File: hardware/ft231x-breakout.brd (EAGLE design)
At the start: 26.7 x 15.2 mm, 27 parts, among them Q1 2N7002PW, U1 FT231XS

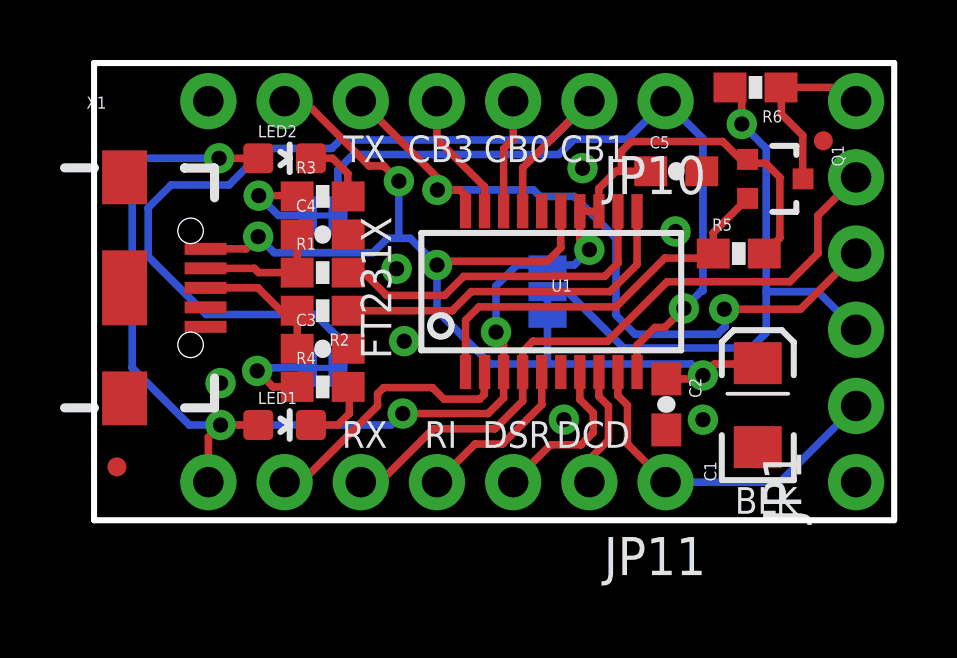
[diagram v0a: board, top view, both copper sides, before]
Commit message: Updated USB with Staking vias
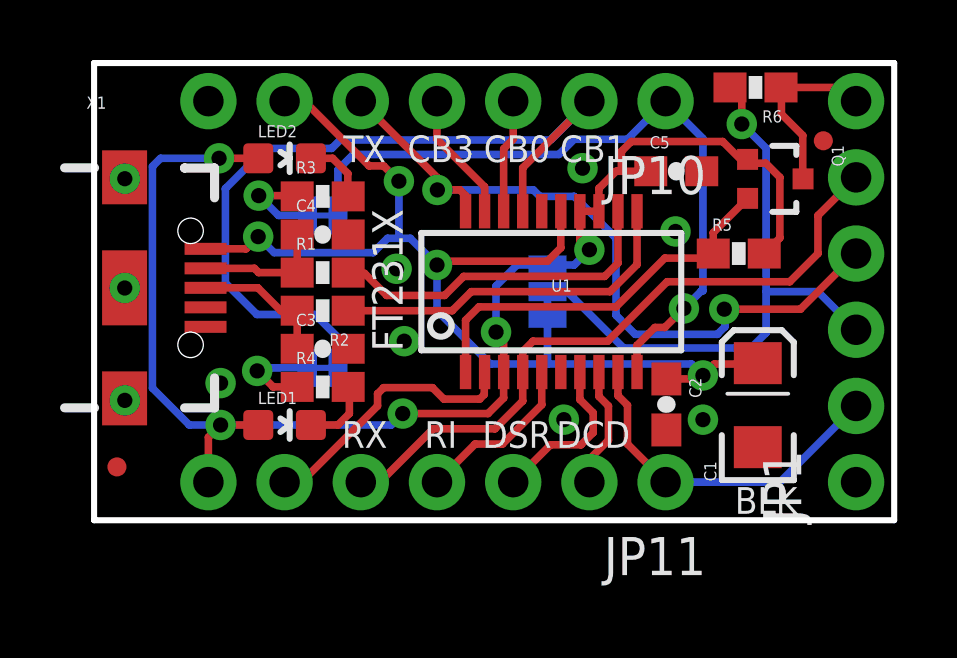
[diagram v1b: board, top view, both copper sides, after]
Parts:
- removed JP2: LOGO-SFENW2, SparkFun-Aesthetics:SFE-NEW-WEB
- added LOGO1: SFE_LOGO_NAME.1_INCH, SparkFun-Aesthetics:SFE_LOGO_NAME_.1
- moved FRAME1 11.7 mm to (-7.62, -12.7)
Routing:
- net RXLED: track 32.6 -> 28.4 mm
- net 3.3V: track 49.5 -> 48.6 mm
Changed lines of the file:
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@@
 <setting verticaltext="up"/>
 </settings>
-<grid distance="0.05" unitdist="inch" unit="inch" style="lines" multiple="1" display="yes" altdistance="0.005" altunitdist="inch" altunit="inch"/>
+<grid distance="0.05" unitdist="inch" unit="inch" style="lines" multiple="1" display="yes" altdistance="0.0001" altunitdist="inch" altunit="inch"/>
 <layers>
 <layer number="1" name="Top" color="4" fill="1" visible="yes" active="yes"/>
@@
 <text x="11.557" y="3.302" size="0.889" layer="21" font="vector" ratio="15" rot="R180" align="bottom-center">RI</text>
 <text x="9.017" y="3.302" size="0.889" layer="21" font="vector" ratio="15" rot="R180" align="bottom-center">RX</text>
-<text x="8.89" y="7.747" size="1.016" layer="21" font="vector" ratio="15" rot="R90" align="top-center">FT231X</text>
+<text x="9.271" y="8.001" size="1.016" layer="21" font="vector" ratio="15" rot="R90" align="top-center">FT231X</text>
 <text x="15.113" y="5.969" size="1.016" layer="22" font="vector" ratio="15" rot="MR0" align="top-center">5V</text>
 <text x="14.986" y="9.271" size="1.016" layer="22" font="vector" ratio="15" rot="MR180" align="top-center">3.3</text>
@@
 </autorouter>
 <elements>
-<element name="FRAME1" library="SparkFun-Aesthetics" package="CREATIVE_COMMONS" value="FRAME-LETTER" x="0" y="-3.81"/>
+<element name="FRAME1" library="SparkFun-Aesthetics" package="CREATIVE_COMMONS" value="FRAME-LETTER" x="-7.62" y="-12.7"/>
 <element name="U1" library="SparkFun-DigitalIC" package="SSOP20_L" value="FT231XS" x="15.24" y="7.62" smashed="yes">
 <attribute name="NAME" x="15.24" y="7.62" size="0.4064" layer="25"/>
-<attribute name="VALUE" x="15.24" y="6.35" size="0.4064" layer="27"/>
+<attribute name="VALUE" value="FTS31XS-U" x="15.24" y="6.35" size="0.4064" layer="27"/>
+<attribute name="PROD_ID" value="IC-11524" x="15.24" y="7.62" size="1.778" layer="27" display="off"/>
 </element>
 <element name="C2" library="SparkFun-Capacitors" package="0603-CAP" value="0.1uF" x="19.0754" y="3.8608" rot="R270">
@@
 <attribute name="VALUE" value="10K" x="22.0472" y="14.4272" size="1.778" layer="27" rot="R180" display="off"/>
 </element>
-<element name="JP2" library="SparkFun-Aesthetics" package="SFE-NEW-WEB" value="LOGO-SFENW2" x="13.843" y="5.842" rot="MR0"/>
 <element name="U$1" library="SparkFun-Aesthetics" package="OSHW-LOGO-S" value="OSHW-LOGOS" x="19.304" y="7.493" smashed="yes" rot="MR0"/>
 <element name="JP3" library="SparkFun-Aesthetics" package="MICRO-FIDUCIAL" value="FIDUCIALUFIDUCIAL" x="0.762" y="1.778"/>
 <element name="JP4" library="SparkFun-Aesthetics" package="MICRO-FIDUCIAL" value="FIDUCIALUFIDUCIAL" x="24.3078" y="12.6492"/>
+<element name="LOGO1" library="SparkFun-Aesthetics" package="SFE_LOGO_NAME_.1" value="SFE_LOGO_NAME.1_INCH" x="12.7" y="5.588" rot="MR0"/>
 </elements>
 <signals>
@@
 <via x="20.2946" y="3.3528" extent="1-16" drill="0.508"/>
 <via x="10.0838" y="8.382" extent="1-16" drill="0.508"/>
+<via x="1.02108125" y="7.741921875" extent="1-16" drill="0.508"/>
+<via x="1.023621875" y="3.995421875" extent="1-16" drill="0.508"/>
+<via x="1.023621875" y="11.384284375" extent="1-16" drill="0.508"/>
 </signal>
 <signal name="VCC">
@@
 <wire x1="22.86" y1="9.4116" x2="22.3384" y2="8.89" width="0.254" layer="1"/>
 <wire x1="4.2164" y1="3.175" x2="3.175" y2="3.175" width="0.254" layer="16"/>
-<wire x1="3.175" y1="3.175" x2="1.27" y2="5.08" width="0.254" layer="16"/>
-<wire x1="1.27" y1="5.08" x2="1.27" y2="11.6586" width="0.254" layer="16"/>
-<wire x1="1.27" y1="11.6586" x2="1.6764" y2="12.065" width="0.254" layer="16"/>
-<wire x1="1.6764" y1="12.065" x2="4.1656" y2="12.065" width="0.254" layer="16"/>
 <wire x1="9.906" y1="3.175" x2="10.287" y2="3.556" width="0.254" layer="16"/>
 <wire x1="3.81" y1="1.27" x2="3.81" y2="2.7686" width="0.254" layer="1"/>
 <wire x1="3.81" y1="2.7686" x2="4.2164" y2="3.175" width="0.254" layer="1"/>
+<wire x1="3.175" y1="3.175" x2="1.945640625" y2="4.404359375" width="0.254" layer="16"/>
+<wire x1="1.945640625" y1="4.404359375" x2="1.945640625" y2="11.795759375" width="0.254" layer="16"/>
+<wire x1="1.945640625" y1="11.795759375" x2="2.21488125" y2="12.065" width="0.254" layer="16"/>
+<wire x1="2.21488125" y1="12.065" x2="4.1656" y2="12.065" width="0.254" layer="16"/>
 </signal>
 <signal name="CBUS3">
@@
 <wire x1="8.128" y1="5.08" x2="8.128" y2="6.096" width="0.254" layer="16"/>
 <wire x1="8.128" y1="6.096" x2="7.366" y2="6.858" width="0.254" layer="16"/>
-<wire x1="7.366" y1="6.858" x2="3.7338" y2="6.858" width="0.254" layer="16"/>
 <wire x1="15.24" y1="12.7" x2="16.51" y2="13.97" width="0.254" layer="16"/>
-<wire x1="3.7338" y1="6.858" x2="1.8034" y2="8.7884" width="0.254" layer="16"/>
-<wire x1="1.8034" y1="8.7884" x2="1.8034" y2="10.414" width="0.254" layer="16"/>
-<wire x1="1.8034" y1="10.414" x2="2.5654" y2="11.176" width="0.254" layer="16"/>
-<wire x1="2.5654" y1="11.176" x2="4.4958" y2="11.176" width="0.254" layer="16"/>
-<wire x1="4.4958" y1="11.176" x2="5.715" y2="12.3952" width="0.254" layer="16"/>
 <wire x1="5.715" y1="12.3952" x2="7.9248" y2="12.3952" width="0.254" layer="16"/>
 <wire x1="7.9248" y1="12.3952" x2="8.2042" y2="12.6746" width="0.254" layer="16"/>
 <wire x1="8.2042" y1="12.6746" x2="15.2146" y2="12.6746" width="0.254" layer="16"/>
 <wire x1="15.2146" y1="12.6746" x2="16.51" y2="13.97" width="0.254" layer="16"/>
+<wire x1="7.366" y1="6.858" x2="5.427978125" y2="6.858" width="0.254" layer="16"/>
+<wire x1="5.427978125" y1="6.858" x2="4.37641875" y2="7.909559375" width="0.254" layer="16"/>
+<wire x1="4.37641875" y1="7.909559375" x2="4.37641875" y2="11.05661875" width="0.254" layer="16"/>
+<wire x1="4.37641875" y1="11.05661875" x2="5.715" y2="12.3952" width="0.254" layer="16"/>
 </signal>
 <signal name="CBUS0">

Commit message: Initial QC CL, Updated Parts, Fixed SCH.
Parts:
- C1: device SparkFun-Passives:EIA3216 -> SparkFun-Capacitors:EIA3216
- moved JP3 11.8 mm to (1.40, 13.6)
- moved JP4 7.49 mm to (24.2, 5.16)
- renumbered LED1 to D1, LED2 to D2
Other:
- board text added: "J. Lindblom"
- board text added: "Revised by: Patrick Alberts"
- board text added: "V10"
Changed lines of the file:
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@@
 <setting verticaltext="up"/>
 </settings>
-<grid distance="0.05" unitdist="inch" unit="inch" style="lines" multiple="1" display="yes" altdistance="0.0001" altunitdist="inch" altunit="inch"/>
+<grid distance="0.05" unitdist="inch" unit="inch" style="lines" multiple="1" display="yes" altdistance="0.005" altunitdist="inch" altunit="inch"/>
 <layers>
 <layer number="1" name="Top" color="4" fill="1" visible="yes" active="yes"/>
@@
 <layer number="47" name="Measures" color="7" fill="1" visible="no" active="yes"/>
 <layer number="48" name="Document" color="7" fill="1" visible="no" active="yes"/>
-<layer number="49" name="Reference" color="7" fill="1" visible="no" active="yes"/>
+<layer number="49" name="Reference" color="7" fill="1" visible="yes" active="yes"/>
 <layer number="50" name="dxf" color="7" fill="1" visible="no" active="no"/>
 <layer number="51" name="tDocu" color="6" fill="1" visible="yes" active="yes"/>
@@
 <layer number="56" name="wert" color="7" fill="1" visible="no" active="no"/>
 <layer number="57" name="tCAD" color="7" fill="1" visible="no" active="no"/>
+<layer number="90" name="Modules" color="5" fill="1" visible="yes" active="yes"/>
 <layer number="91" name="Nets" color="2" fill="1" visible="no" active="no"/>
 <layer number="92" name="Busses" color="1" fill="1" visible="no" active="no"/>
@@
 <text x="8.382" y="5.08" size="0.889" layer="22" font="vector" ratio="15" rot="MR180" align="center-left">CB1</text>
 <text x="8.382" y="10.16" size="0.889" layer="22" font="vector" ratio="15" rot="MR180" align="center-left">CB2</text>
+<dimension x1="-7.62" y1="0" x2="-7.62" y2="15.24" x3="-8.89" y3="7.62" textsize="1.778" textratio="15" layer="47"/>
+<dimension x1="0" y1="20.32" x2="26.67" y2="20.32" x3="13.335" y3="21.59" textsize="1.778" textratio="15" layer="47"/>
+<text x="18.669" y="-12.7" size="1.6764" layer="51" font="vector" ratio="12">J. Lindblom</text>
+<text x="4.191" y="-15.24" size="1.6764" layer="51" font="vector" ratio="12">Revised by: Patrick Alberts</text>
+<text x="0.635" y="0.508" size="0.8128" layer="16" font="vector" ratio="12" rot="MR90">V10</text>
 </plain>
 <attributes>
@@
 <attribute name="VALUE" value="47pF" x="7.62" y="9.525" size="1.778" layer="27" display="off"/>
 </element>
-<element name="R1" library="SparkFun-Resistors" package="0603-RES" value="27" x="7.62" y="8.255"/>
-<element name="R2" library="SparkFun-Resistors" package="0603-RES" value="27" x="7.62" y="6.985" rot="R180"/>
+<element name="R1" library="SparkFun-Resistors" package="0603-RES" value="27" x="7.62" y="8.255">
+<attribute name="PROD_ID" value="RES-09334" x="7.62" y="8.255" size="1.778" layer="27" display="off"/>
+</element>
+<element name="R2" library="SparkFun-Resistors" package="0603-RES" value="27" x="7.62" y="6.985" rot="R180">
+<attribute name="PROD_ID" value="RES-09334" x="7.62" y="6.985" size="1.778" layer="27" rot="R180" display="off"/>
+</element>
 <element name="X1" library="SparkFun-Connectors" package="USB-AB-MICRO-SMD_V03" value="" x="1.016" y="7.747">
 <attribute name="PROD_ID" value="CONN-11794" x="20.066" y="-4.953" size="1.778" layer="27" display="off"/>
@@
 <element name="JP1" library="SparkFun-Connectors" package="1X06_NS" value="" x="25.4" y="1.27" rot="R90"/>
 <element name="SJ1" library="SparkFun-Passives" package="SJ_3" value="" x="15.113" y="7.62" rot="MR270"/>
-<element name="C1" library="SparkFun-Passives" package="EIA3216" value="10uF" x="22.1234" y="3.8354" rot="R90"/>
-<element name="LED1" library="SparkFun-LED" package="LED-0603" value="RED" x="6.35" y="3.175" rot="R270"/>
-<element name="LED2" library="SparkFun-LED" package="LED-0603" value="YELLOW" x="6.35" y="12.065" rot="R270">
+<element name="C1" library="SparkFun-Capacitors" package="EIA3216" value="10uF" x="22.1234" y="3.8354" rot="R90">
+<attribute name="PROD_ID" value="CAP-00811" x="22.1234" y="3.8354" size="1.778" layer="27" rot="R90" display="off"/>
+<attribute name="VALUE" value="10uF" x="22.1234" y="3.8354" size="1.778" layer="27" rot="R90" display="off"/>
+</element>
+<element name="D1" library="SparkFun-LED" package="LED-0603" value="RED" x="6.35" y="3.175" rot="R270">
+<attribute name="PROD_ID" value="DIO-00819" x="6.35" y="3.175" size="1.778" layer="27" rot="R270" display="off"/>
+<attribute name="VALUE" value="RED" x="6.35" y="3.175" size="1.778" layer="27" rot="R270" display="off"/>
+</element>
+<element name="D2" library="SparkFun-LED" package="LED-0603" value="YELLOW" x="6.35" y="12.065" rot="R270">
 <attribute name="PROD_ID" value="DIO-09003" x="6.35" y="12.065" size="1.778" layer="27" rot="R270" display="off"/>
 </element>
@@
 <element name="JP10" library="SparkFun-Connectors" package="1X07_NS" value="" x="19.05" y="13.97" rot="R180"/>
 <element name="JP11" library="SparkFun-Connectors" package="1X07_NS" value="" x="19.05" y="1.27" rot="R180"/>
-<element name="Q1" library="SparkFun-DiscreteSemi" package="SOT323" value="2N7002PW" x="22.7076" y="11.3792" rot="R270"/>
+<element name="Q1" library="SparkFun-DiscreteSemi" package="SOT323" value="2N7002PW" x="22.7076" y="11.3792" rot="R270">
+<attribute name="PROD_ID" value="TRANS-11151" x="22.7076" y="11.3792" size="1.778" layer="27" rot="R270" display="off"/>
+</element>
 <element name="R5" library="SparkFun-Resistors" package="0603-RES" value="10k" x="21.4884" y="8.89">
 <attribute name="PROD_ID" value="RES-00824" x="21.4884" y="8.89" size="1.778" layer="27" display="off"/>
@@
 </element>
 <element name="U$1" library="SparkFun-Aesthetics" package="OSHW-LOGO-S" value="OSHW-LOGOS" x="19.304" y="7.493" smashed="yes" rot="MR0"/>
-<element name="JP3" library="SparkFun-Aesthetics" package="MICRO-FIDUCIAL" value="FIDUCIALUFIDUCIAL" x="0.762" y="1.778"/>
-<element name="JP4" library="SparkFun-Aesthetics" package="MICRO-FIDUCIAL" value="FIDUCIALUFIDUCIAL" x="24.3078" y="12.6492"/>
+<element name="JP3" library="SparkFun-Aesthetics" package="MICRO-FIDUCIAL" value="FIDUCIALUFIDUCIAL" x="1.397" y="13.589"/>
+<element name="JP4" library="SparkFun-Aesthetics" package="MICRO-FIDUCIAL" value="FIDUCIALUFIDUCIAL" x="24.1808" y="5.1562"/>
 <element name="LOGO1" library="SparkFun-Aesthetics" package="SFE_LOGO_NAME_.1" value="SFE_LOGO_NAME.1_INCH" x="12.7" y="5.588" rot="MR0"/>
 </elements>
@@
 <wire x1="16.1925" y1="9.3345" x2="16.51" y2="9.017" width="0.254" layer="1"/>
 <via x="13.3985" y="6.2738" extent="1-16" drill="0.508"/>
-<contactref element="LED2" pad="A"/>
-<contactref element="LED1" pad="A"/>
+<contactref element="D2" pad="A"/>
+<contactref element="D1" pad="A"/>
 <via x="4.2164" y="3.175" extent="1-16" drill="0.508"/>
 <via x="10.287" y="3.556" extent="1-16" drill="0.508"/>
@@
 </signal>
 <signal name="N$5">
-<contactref element="LED2" pad="C"/>
+<contactref element="D2" pad="C"/>
 <contactref element="R3" pad="2"/>
 <wire x1="7.227" y1="12.065" x2="7.9502" y2="12.065" width="0.254" layer="1"/>
@@
 </signal>
 <signal name="N$6">
-<contactref element="LED1" pad="C"/>
+<contactref element="D1" pad="C"/>
 <contactref element="R4" pad="2"/>
 <wire x1="8.37" y1="4.345" x2="8.47" y2="4.445" width="0.254" layer="1"/>

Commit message: Silk Change
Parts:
- moved FRAME1 4.02 mm to (-11.4, -11.4)
- moved C5 0.13 mm to (19.3, 11.6)
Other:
- board text added: "V01"
- board text removed: "V10"
